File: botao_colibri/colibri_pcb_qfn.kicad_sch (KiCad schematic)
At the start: 6 parts, among them J2 TC2030, U1 ME54BS12

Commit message: Desenho dos pads do botão principal, GPIOS acessíveis (adição de conectores para as GPIOS sem uso atual), retrabalho de trilhas.
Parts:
- added J5, J6, J7: Conn_01x06, Connector_PinHeader_2.54mm:PinHeader_1x06_P2.54mm_Vertical, symbol Connector_Generic:Conn_01x06
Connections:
- net GND: now also J5.1 (Pin_1)
- net P0.00: now reaches U1.12 (P0.00)
- net P0.00: now also J6.1 (Pin_1)
- net P1.02: now reaches U1.7 (P1.02/NFC1)
- net P1.02: now also J5.3 (Pin_3)
- net P0.04: now reaches U1.A6 (P0.04)
- net P0.04: now also J6.2 (Pin_2)
- net P1.09: now reaches U1.B1 (P1.09)
- net P1.09: now also J5.5 (Pin_5)
- net P2.09: now reaches U1.B6 (P2.09)
- net P2.09: now also J7.5 (Pin_5)
- net P1.10: now reaches U1.C1 (P1.10)
- net P1.10: now also J5.6 (Pin_6)
- net P2.10: now reaches U1.C6 (P2.10)
- net P2.10: now also J7.6 (Pin_6)
- net P2.00: now reaches U1.D1 (P2.00)
- net P2.00: now also J6.3 (Pin_3)
- net P2.08: now reaches U1.D5 (P2.08)
- net P2.08: now also J7.4 (Pin_4)
- net P2.07: now reaches U1.D6 (P2.07)
- net P2.07: now also J7.3 (Pin_3)
- net P1.08: now reaches U1.E1 (P1.08)
- net P1.08: now also J5.4 (Pin_4)
- net P2.05: now reaches U1.E5 (P2.05)
- net P2.05: now also J7.1 (Pin_1)
- net P2.06: now reaches U1.E6 (P2.06)
- net P2.06: now also J7.2 (Pin_2)
- net P1.07: now reaches U1.F1 (P1.07/AIN3)
- net P1.07: now also J5.2 (Pin_2)
- net P2.01: now reaches U1.F3 (P2.01)
- net P2.01: now also J6.4 (Pin_4)
- net P2.03: now reaches U1.F4 (P2.03)
- net P2.03: now also J6.6 (Pin_6)
- net P2.02: now reaches U1.F5 (P2.02)
- net P2.02: now also J6.5 (Pin_5)
- no-connect marks 19 -> 2

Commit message: continuação
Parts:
- removed J7: Conn_01x06, Connector_PinHeader_2.54mm:PinHeader_1x06_P2.54mm_Vertical, symbol Connector_Generic:Conn_01x06
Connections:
- net GND: no longer J5.1 (Pin_1)
- net P0.00: no longer J6.1 (Pin_1)
- net P0.04: no longer J6.2 (Pin_2)
- net P1.02: now also J6.1 (Pin_1); no longer J5.3 (Pin_3)
- net P1.07: now also J6.6 (Pin_6); no longer J5.2 (Pin_2)
- net P1.08: now also J6.5 (Pin_5); no longer J5.4 (Pin_4)
- net P1.09: now also J6.2 (Pin_2); no longer J5.5 (Pin_5)
- net P1.10: now also J6.3 (Pin_3); no longer J5.6 (Pin_6)
- net P2.00: now also J6.4 (Pin_4); no longer J6.3 (Pin_3)
- net P2.01: now also J5.1 (Pin_1); no longer J6.4 (Pin_4)
- net P2.02: now also J5.3 (Pin_3); no longer J6.5 (Pin_5)
- net P2.03: now also J5.2 (Pin_2); no longer J6.6 (Pin_6)
- net P2.05: now also J5.4 (Pin_4)
- net P2.06: now also J5.6 (Pin_6)
- net P2.08: now also J5.5 (Pin_5)

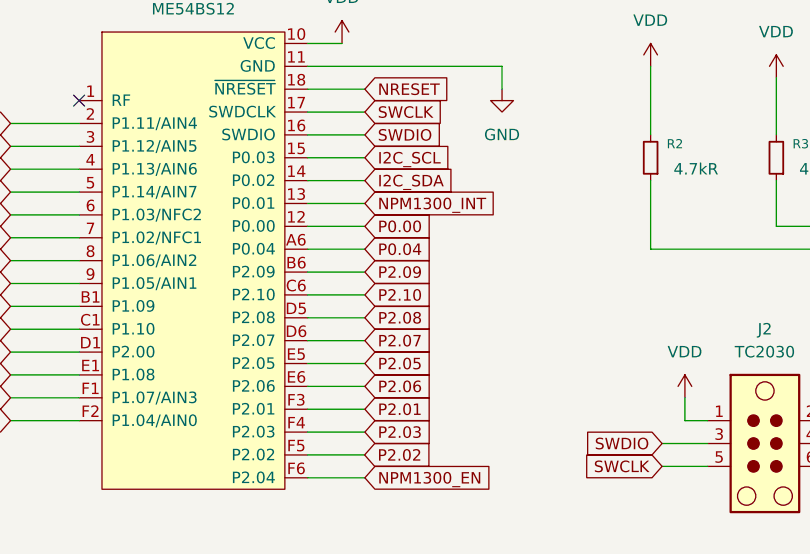
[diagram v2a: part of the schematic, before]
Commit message: Mudanças de posição de componentes e trilhas
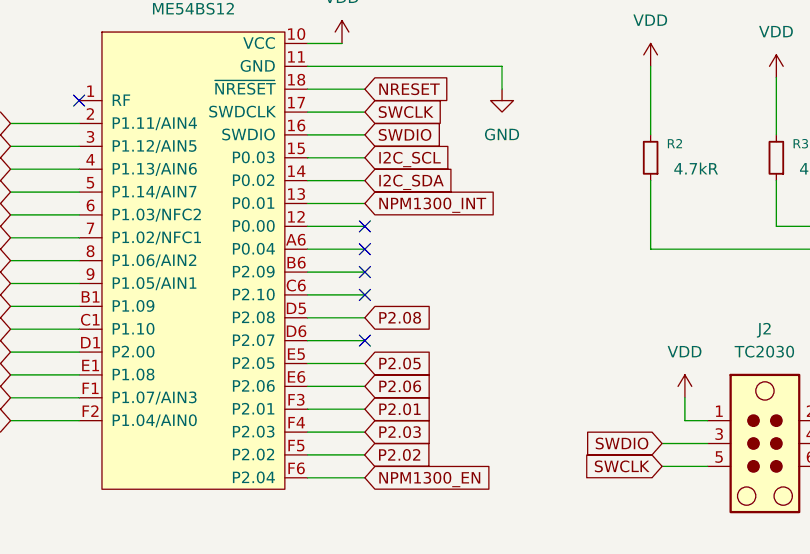
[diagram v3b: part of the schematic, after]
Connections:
- net P0.00: no longer names the net of U1.12 (P0.00)
- net P0.04: no longer names the net of U1.A6 (P0.04)
- net P2.07: no longer names the net of U1.D6 (P2.07)
- net P2.09: no longer names the net of U1.B6 (P2.09)
- net P2.10: no longer names the net of U1.C6 (P2.10)
- no-connect marks 2 -> 7
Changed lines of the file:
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@@
+	)
+	(no_connect
+		(at 158.75 91.44)
 	)
 	(no_connect
@@
 		(at 127 72.39)
 	)
+	(no_connect
+		(at 158.75 86.36)
+	)
+	(no_connect
+		(at 158.75 93.98)
+	)
+	(no_connect
+		(at 158.75 99.06)
+	)
+	(no_connect
+		(at 158.75 88.9)
+	)
 	(wire
 		(pts
@@
 		)
 	)
-	(global_label "P0.04"
-		(shape input)
-		(at 158.75 88.9 0)
-		(fields_autoplaced yes)
-		(effects
-			(font
-				(size 1.27 1.27)
-			)
-			(justify left)
-		)
-		(property "Intersheetrefs" "${INTERSHEET_REFS}"
-			(at 167.2385 88.9 0)
-			(hide yes)
-			(show_name no)
-			(do_not_autoplace no)
-			(effects
-				(font
-					(size 1.27 1.27)
-				)
-				(justify left)
-			)
-		)
-	)
 	(global_label "P2_SQUARE_WAVE"
 		(shape input)
@@
 		)
 	)
-	(global_label "P2.10"
-		(shape input)
-		(at 158.75 93.98 0)
-		(fields_autoplaced yes)
-		(effects
-			(font
-				(size 1.27 1.27)
-			)
-			(justify left)
-		)
-		(property "Intersheetrefs" "${INTERSHEET_REFS}"
-			(at 167.2385 93.98 0)
-			(hide yes)
-			(show_name no)
-			(do_not_autoplace no)
-			(effects
-				(font
-					(size 1.27 1.27)
-				)
-				(justify left)
-			)
-		)
-	)
 	(global_label "P1.07"
 		(shape input)
@@
 		)
 	)
-	(global_label "P2.09"
-		(shape input)
-		(at 158.75 91.44 0)
-		(fields_autoplaced yes)
-		(effects
-			(font
-				(size 1.27 1.27)
-			)
-			(justify left)
-		)
-		(property "Intersheetrefs" "${INTERSHEET_REFS}"
-			(at 167.2385 91.44 0)
-			(hide yes)
-			(show_name no)
-			(do_not_autoplace no)
-			(effects
-				(font
-					(size 1.27 1.27)
-				)
-				(justify left)
-			)
-		)
-	)
 	(global_label "P1.08"
 		(shape input)
@@
 		)
 	)
-	(global_label "P2.07"
-		(shape input)
-		(at 158.75 99.06 0)
-		(fields_autoplaced yes)
-		(effects
-			(font
-				(size 1.27 1.27)
-			)
-			(justify left)
-		)
-		(property "Intersheetrefs" "${INTERSHEET_REFS}"
-			(at 167.2385 99.06 0)
-			(hide yes)
-			(show_name no)
-			(do_not_autoplace no)
-			(effects
-				(font
-					(size 1.27 1.27)
-				)
-				(justify left)
-			)
-		)
-	)
 	(global_label "P1.02"
 		(shape input)
@@
 			)
 		)
-	)
-	(global_label "P0.00"
-		(shape input)
-		(at 158.75 86.36 0)
-		(fields_autoplaced yes)
-		(effects
-			(font
-				(size 1.27 1.27)
-			)
-			(justify left)
-		)
-		(property "Intersheetrefs" "${INTERSHEET_REFS}"
-			(at 167.2385 86.36 0)
-			(hide yes)
-			(show_name no)
-			(do_not_autoplace no)
-			(effects
-				(font
-					(size 1.27 1.27)
-				)
-				(justify left)
-			)
-		)
